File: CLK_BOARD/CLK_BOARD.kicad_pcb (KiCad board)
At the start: 2 copper layers, 18 parts, among them J4 PWR, U1 LMK00804BPW, U2 SN74LVC1G74DCUR, U3 LMK00804BPW, U4 TPS7A9101DSKR, X1 TB612-100.0M

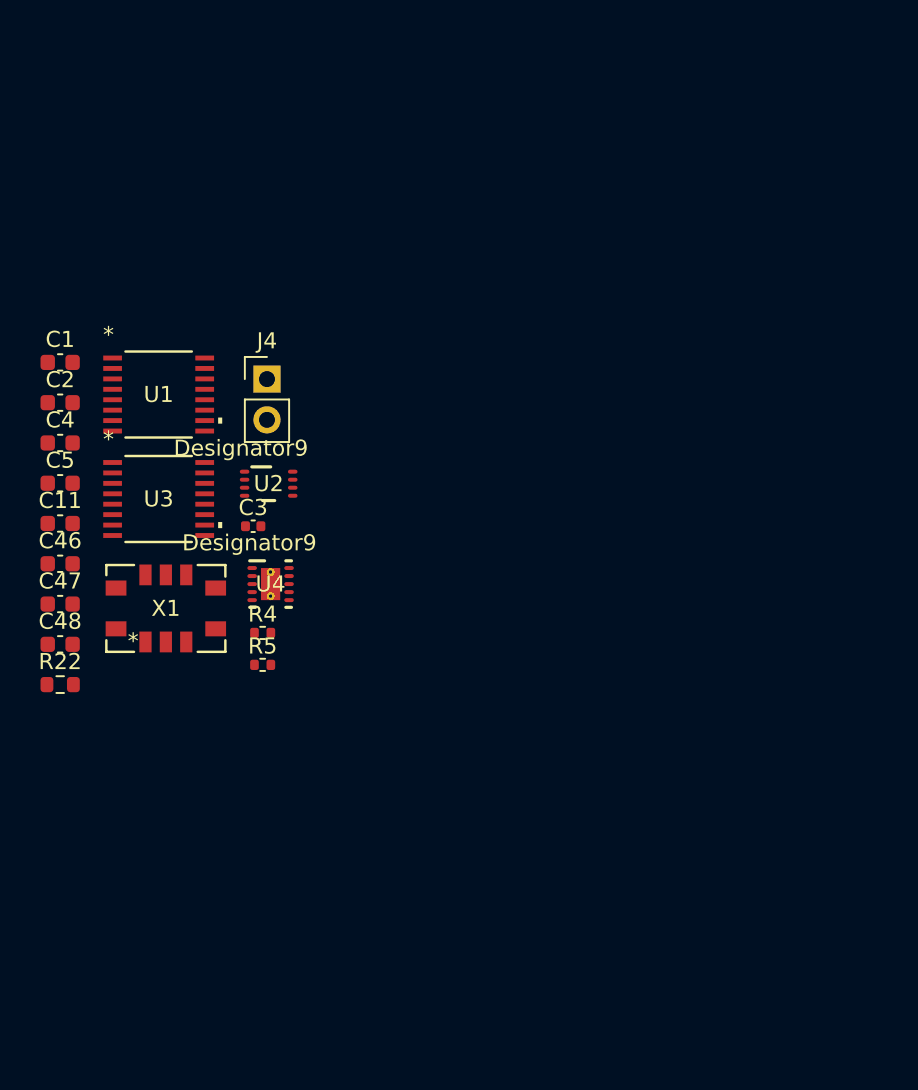
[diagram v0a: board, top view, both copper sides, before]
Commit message: finished clock board schematic
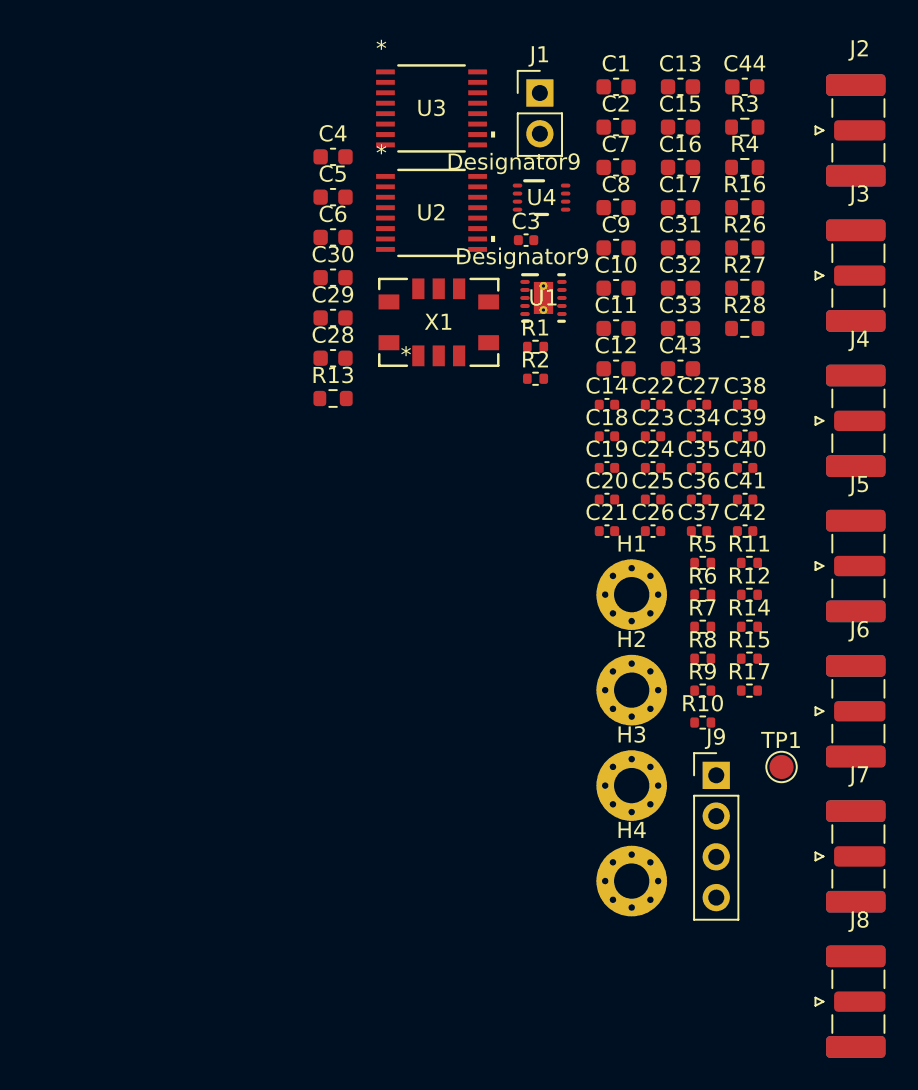
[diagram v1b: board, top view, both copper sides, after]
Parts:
- added C10: 0.1uF, Capacitor_SMD:C_0603_1608Metric, F.Cu at (133.0, 71.5)
- added C11: 0.1uF, Capacitor_SMD:C_0603_1608Metric, F.Cu at (133.0, 74.0)
- added C12: 10uF, Capacitor_SMD:C_0603_1608Metric, F.Cu at (133.0, 76.5)
- added C13: 1uF, Capacitor_SMD:C_0603_1608Metric, F.Cu at (137.0, 58.9)
- added C14: 10nF, Capacitor_SMD:C_0402_1005Metric, F.Cu at (132.4, 78.7)
- added C15: 0.1uF, Capacitor_SMD:C_0603_1608Metric, F.Cu at (137.0, 61.4)
- added C16: 0.1uF, Capacitor_SMD:C_0603_1608Metric, F.Cu at (137.0, 64.0)
- added C17: 0.1uF, Capacitor_SMD:C_0603_1608Metric, F.Cu at (137.0, 66.5)
- added C18: 10nF, Capacitor_SMD:C_0402_1005Metric, F.Cu at (132.4, 80.7)
- added C19: 10nF, Capacitor_SMD:C_0402_1005Metric, F.Cu at (132.4, 82.7)
- added C20: 15pF, Capacitor_SMD:C_0402_1005Metric, F.Cu at (132.4, 84.7)
- added C21: 15pF, Capacitor_SMD:C_0402_1005Metric, F.Cu at (132.4, 86.6)
- added C22: 10nF, Capacitor_SMD:C_0402_1005Metric, F.Cu at (135.3, 78.7)
- added C23: 10nF, Capacitor_SMD:C_0402_1005Metric, F.Cu at (135.3, 80.7)
- added C24: 10nF, Capacitor_SMD:C_0402_1005Metric, F.Cu at (135.3, 82.7)
- added C25: 10nF, Capacitor_SMD:C_0402_1005Metric, F.Cu at (135.3, 84.7)
- added C26: 15pF, Capacitor_SMD:C_0402_1005Metric, F.Cu at (135.3, 86.6)
- added C27: 15pF, Capacitor_SMD:C_0402_1005Metric, F.Cu at (138.2, 78.7)
- added C31: 10uF, Capacitor_SMD:C_0603_1608Metric, F.Cu at (137.0, 69.0)
- added C32: 1uF, Capacitor_SMD:C_0603_1608Metric, F.Cu at (137.0, 71.5)
- added C33: 0.1uF, Capacitor_SMD:C_0603_1608Metric, F.Cu at (137.0, 74.0)
- added C34: 10nF, Capacitor_SMD:C_0402_1005Metric, F.Cu at (138.2, 80.7)
- added C35: 10nF, Capacitor_SMD:C_0402_1005Metric, F.Cu at (138.2, 82.7)
- added C36: 10nF, Capacitor_SMD:C_0402_1005Metric, F.Cu at (138.2, 84.7)
- added C37: 10nF, Capacitor_SMD:C_0402_1005Metric, F.Cu at (138.2, 86.6)
- added C38: 10nF, Capacitor_SMD:C_0402_1005Metric, F.Cu at (141.0, 78.7)
- added C39: 10nF, Capacitor_SMD:C_0402_1005Metric, F.Cu at (141.0, 80.7)
- added C40: 10nF, Capacitor_SMD:C_0402_1005Metric, F.Cu at (141.0, 82.7)
- added C41: 15pF, Capacitor_SMD:C_0402_1005Metric, F.Cu at (141.0, 84.7)
- added C42: 15pF, Capacitor_SMD:C_0402_1005Metric, F.Cu at (141.0, 86.6)
- added C43: 0.1uF, Capacitor_SMD:C_0603_1608Metric, F.Cu at (137.0, 76.5)
- added C44: 0.1uF, Capacitor_SMD:C_0603_1608Metric, F.Cu at (141.0, 58.9)
- added C7: 10uF, Capacitor_SMD:C_0603_1608Metric, F.Cu at (133.0, 64.0)
- added C8: 1uF, Capacitor_SMD:C_0603_1608Metric, F.Cu at (133.0, 66.5)
- added C9: 0.1uF, Capacitor_SMD:C_0603_1608Metric, F.Cu at (133.0, 69.0)
- added H1: MountingHole_Pad, MountingHole:MountingHole_2.2mm_M2_Pad_Via, F.Cu at (134.0, 90.6)
- added H2: MountingHole_Pad, MountingHole:MountingHole_2.2mm_M2_Pad_Via, F.Cu at (134.0, 96.5)
- added H3: MountingHole_Pad, MountingHole:MountingHole_2.2mm_M2_Pad_Via, F.Cu at (134.0, 102.5)
- added H4: MountingHole_Pad, MountingHole:MountingHole_2.2mm_M2_Pad_Via, F.Cu at (134.0, 108.4)
- added J2: OUT_50M_1, Connector_Coaxial:SMA_Samtec_SMA-J-P-H-ST-EM1_EdgeMount, F.Cu at (148.2, 61.6)
- added J3: OUT_50M_2, Connector_Coaxial:SMA_Samtec_SMA-J-P-H-ST-EM1_EdgeMount, F.Cu at (148.2, 70.7)
- added J4: OUT_50M_3, Connector_Coaxial:SMA_Samtec_SMA-J-P-H-ST-EM1_EdgeMount, F.Cu at (148.2, 79.7)
- added J5: OUT_50M_4, Connector_Coaxial:SMA_Samtec_SMA-J-P-H-ST-EM1_EdgeMount, F.Cu at (148.2, 88.8)
- added J6: OUT_100M_3, Connector_Coaxial:SMA_Samtec_SMA-J-P-H-ST-EM1_EdgeMount, F.Cu at (148.2, 97.8)
- added J7: OUT_100M_2, Connector_Coaxial:SMA_Samtec_SMA-J-P-H-ST-EM1_EdgeMount, F.Cu at (148.2, 106.9)
- added J8: OUT_100M_1, Connector_Coaxial:SMA_Samtec_SMA-J-P-H-ST-EM1_EdgeMount, F.Cu at (148.2, 115.9)
- added J9: Conn_01x04, Connector_PinHeader_2.54mm:PinHeader_1x04_P2.54mm_Vertical, F.Cu at (139.2, 101.8)
- added R10: 43, Resistor_SMD:R_0402_1005Metric, F.Cu at (138.4, 98.5)
- added R11: 43, Resistor_SMD:R_0402_1005Metric, F.Cu at (141.3, 88.6)
- added R12: 43, Resistor_SMD:R_0402_1005Metric, F.Cu at (141.3, 90.6)
- added R14: 0, Resistor_SMD:R_0402_1005Metric, F.Cu at (141.3, 92.6)
- added R15: 0, Resistor_SMD:R_0402_1005Metric, F.Cu at (141.3, 94.6)
- added R16: 0, Resistor_SMD:R_0603_1608Metric, F.Cu at (141.0, 66.5)
- added R17: 0, Resistor_SMD:R_0402_1005Metric, F.Cu at (141.3, 96.6)
- added R26: 10k, Resistor_SMD:R_0603_1608Metric, F.Cu at (141.0, 69.0)
- added R27: 10k, Resistor_SMD:R_0603_1608Metric, F.Cu at (141.0, 71.5)
- added R28: 100k, Resistor_SMD:R_0603_1608Metric, F.Cu at (141.0, 74.0)
- added R3: 0, Resistor_SMD:R_0603_1608Metric, F.Cu at (141.0, 61.4)
- added R4: 0, Resistor_SMD:R_0603_1608Metric, F.Cu at (141.0, 64.0)
- added R5: 43, Resistor_SMD:R_0402_1005Metric, F.Cu at (138.4, 88.6)
- added R6: 43, Resistor_SMD:R_0402_1005Metric, F.Cu at (138.4, 90.6)
- added R7: 43, Resistor_SMD:R_0402_1005Metric, F.Cu at (138.4, 92.6)
- added R8: 0, Resistor_SMD:R_0402_1005Metric, F.Cu at (138.4, 94.6)
- added R9: 43, Resistor_SMD:R_0402_1005Metric, F.Cu at (138.4, 96.6)
- added TP1: PG, TestPoint:TestPoint_Pad_D1.5mm, F.Cu at (143.3, 101.3)
- C1: value 0.1uF -> 10uF
- C2: value 10uF -> 0.1uF
- moved C1 38.7 mm to (133.0, 58.9)
- moved C2 38.7 mm to (133.0, 61.4)
- moved U4 24.6 mm to (128.4, 65.8)
- moved U3 24.6 mm to (121.5, 60.3)
- moved C29 24.6 mm to (115.4, 73.3)
- moved C5 24.6 mm to (115.4, 65.8)
- moved R1 24.6 mm to (128.0, 75.1)
- moved R2 24.6 mm to (128.0, 77.1)
- moved U1 24.6 mm to (128.5, 72.1)
- moved U2 24.6 mm to (121.5, 66.8)
- moved X1 24.6 mm to (122.0, 73.6)
- moved C28 24.6 mm to (115.4, 75.8)
- moved C3 24.6 mm to (127.4, 68.5)
- moved C30 24.6 mm to (115.4, 70.8)
- moved C4 24.6 mm to (115.4, 63.3)
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- renumbered C48 to C28, C47 to C29, C46 to C30, C11 to C6, J4 to J1, R4 to R1, R22 to R13, R5 to R2, U4 to U1, U3 to U2, U1 to U3, U2 to U4
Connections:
- U1 pad 5: GND -> Net-(U1-PG)
- U2 pad 4: unconnected-(U3-CLK_EN-Pad4) -> /nMUTE
- U2 pad 7: unconnected-(U3-CLK_SEL-Pad7) -> GND
- U2 pad 8: Net-(U2-D) -> Net-(U2-LVCMOS_CLK)
- U3 pad 16: Net-(U1-Q0) -> Net-(U3-Q0)
- U3 pad 4: unconnected-(U1-CLK_EN-Pad4) -> /nMUTE
- U3 pad 8: Net-(U1-LVCMOS_CLK) -> /OSC_OUT
- U4 pad 1: Net-(U1-Q0) -> Net-(U4-CLK)
- U4 pad 2: Net-(U2-D) -> Net-(U4-D)
- U4 pad 3: Net-(U2-D) -> Net-(U4-D)
- U4 pad 5: unconnected-(U2-Q-Pad5) -> Net-(U4-Q)
- U4 pad 6: unconnected-(U2-CLR_N-Pad6) -> /nRST
- U4 pad 7: unconnected-(U2-PRE_N-Pad7) -> Net-(U4-PRE_N)
- U4 pad 8: unconnected-(U2-VCC-Pad8) -> Net-(U4-VCC)
- X1 pad 5: Net-(U1-LVCMOS_CLK) -> Net-(X1-OUTPUT)

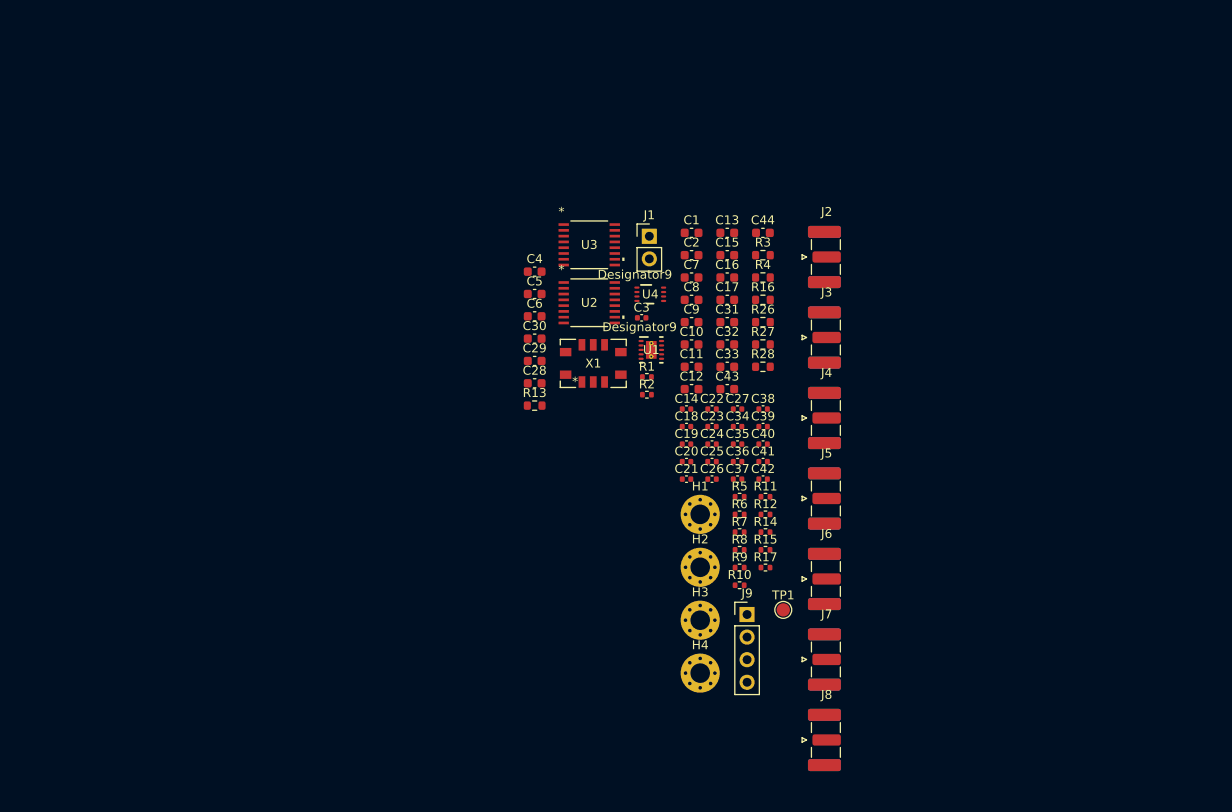
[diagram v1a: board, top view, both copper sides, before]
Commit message: started layout of clk distribution board
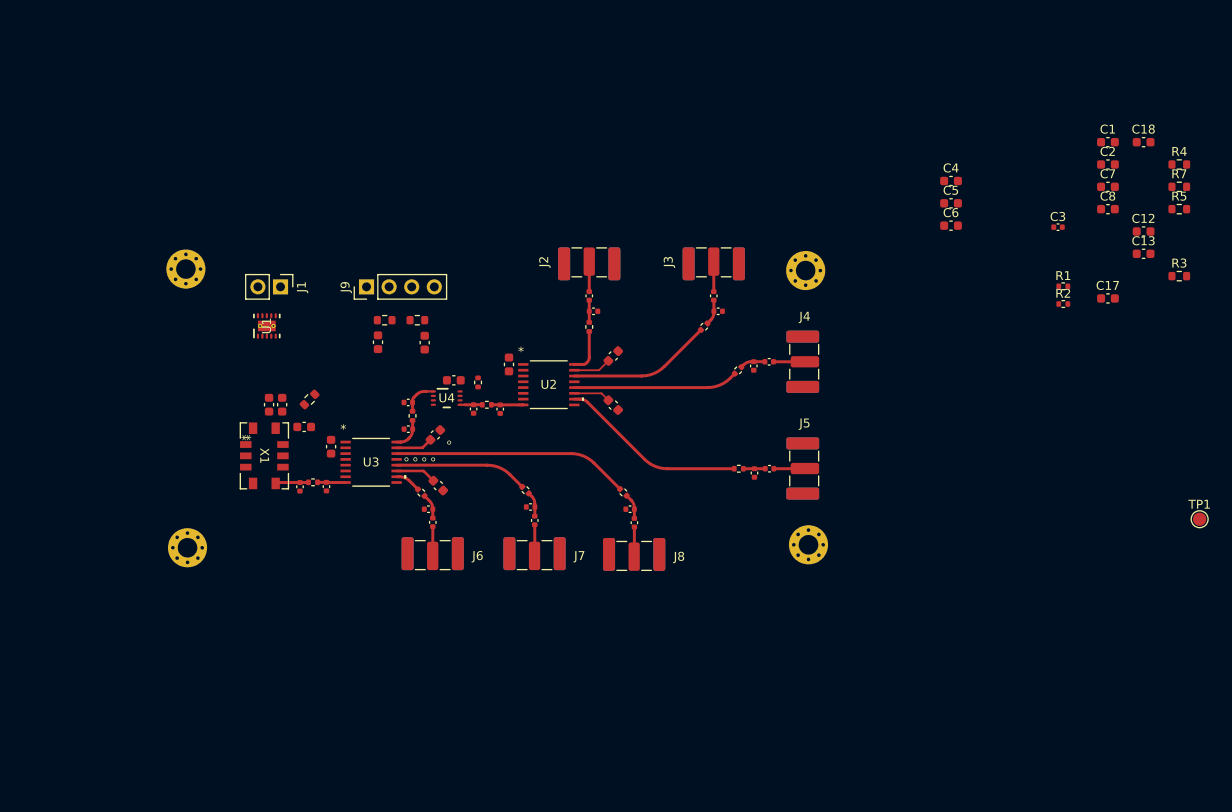
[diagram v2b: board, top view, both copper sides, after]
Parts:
- removed the C29 at (115.4, 73.3)
- removed the C30 at (115.4, 70.8)
- added C43: 0.1uF, Capacitor_SMD:C_0603_1608Metric, F.Cu at (87.0, 78.2)
- added C44: 10nF, Capacitor_SMD:C_0603_1608Metric, F.Cu at (85.5, 78.2)
- moved H1 64.1 mm to (76.2, 63.0)
- moved H3 58.2 mm to (76.3, 94.3)
- moved J9 56.5 mm to (96.5, 65.0), turned to 90 degrees
- moved R20 51.2 mm to (90.4, 87.0)
- moved C1 47.9 mm to (179.8, 48.7)
- moved C12 47.9 mm to (183.8, 58.8)
- moved C13 47.9 mm to (183.8, 61.3)
- moved C17 47.9 mm to (179.8, 66.3)
- moved C18 47.9 mm to (183.8, 48.7)
- moved C2 47.9 mm to (179.8, 51.2)
- moved C3 47.9 mm to (174.2, 58.3)
- moved C4 47.9 mm to (162.2, 53.1)
- moved C5 47.9 mm to (162.2, 55.6)
- moved C6 47.9 mm to (162.2, 58.1)
- moved C7 47.9 mm to (179.8, 53.8)
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- renumbered C31 to C12, C32 to C13, C33 to C14, C14 to C15, C34 to C16, C12 to C17, C13 to C18, C15 to C19, C16 to C20, C17 to C21, C18 to C22, C35 to C23, C20 to C24, C21 to C25, C41 to C26, C42 to C27, C19 to C28, C36 to C29, C22 to C30, C37 to C31, C40 to C32, C39 to C33, C38 to C34, C23 to C35, C24 to C36, C25 to C37, C44 to C38, C43 to C39, C26 to C40, C27 to C41, C28 to C42, R17 to R10, R7 to R11, R15 to R12, R9 to R13, R10 to R14, R11 to R15, R12 to R16, R26 to R17, R27 to R18, R13 to R19, R14 to R20, R28 to R3, R3 to R4, R16 to R5, R5 to R6, R4 to R7, R6 to R8, R8 to R9
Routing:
- net Net-(U3-Q1): track 0.00 -> 26.6 mm
- net Net-(U2-Q3): track 0.00 -> 21.0 mm
- net Net-(U2-Q2): track 0.00 -> 18.5 mm
- net Net-(U2-Q1): track 0.00 -> 16.2 mm
- net Net-(U3-Q2): track 0.00 -> 15.0 mm
- net Net-(U3-VDD): track 0.00 -> 8.77 mm
- net Net-(U2-VDD): track 0.00 -> 8.42 mm
- net Net-(U2-Q0): track 0.00 -> 5.05 mm
- net Net-(U4-CLK): track 0.00 -> 4.02 mm
- net Net-(X1-OUTPUT): track 0.00 -> 3.74 mm
- net Net-(U3-Q0): track 0.00 -> 3.62 mm
- net Net-(U2-LVCMOS_CLK): track 0.00 -> 3.59 mm
- net Net-(J4-In): track 0.00 -> 3.54 mm
- net Net-(J7-In): track 0.00 -> 3.51 mm
- net Net-(J5-In): track 0.00 -> 3.51 mm
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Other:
- copper layers 2 -> 4

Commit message: moved from TSSOP to QFN to make the pcb smaller, will have to restart layout
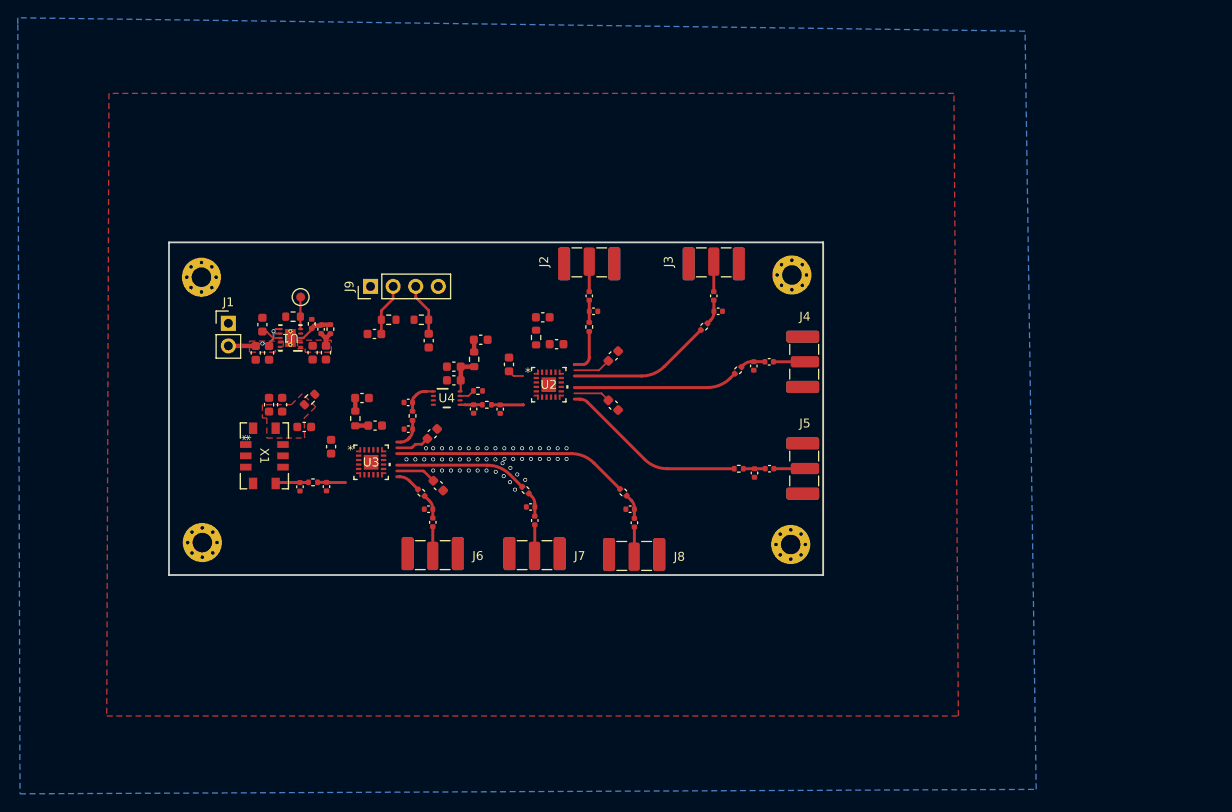
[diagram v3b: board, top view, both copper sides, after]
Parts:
- U2, U3: value LMK00804BPW -> LMK00804BQWRGTRQ1; footprint Snapeda:PW16_TEX-L -> Snapeda:VQFN16_RGT_TEX
- moved TP1 104.1 mm to (89.0, 66.2)
- moved R3 99.7 mm to (88.2, 68.3)
- moved C2 98.1 mm to (84.0, 72.4), turned to -90 degrees
- moved C1 97.2 mm to (85.5, 72.4), turned to -90 degrees
- moved R7 96.2 mm to (95.2, 79.8), turned to -90 degrees
- moved C18 92.1 mm to (97.4, 80.6)
- moved C17 84.6 mm to (96.0, 77.5)
- moved R2 84.5 mm to (90.3, 69.2), turned to 90 degrees
- moved C3 83.6 mm to (91.3, 69.8), turned to 90 degrees
- moved R1 82.5 mm to (92.4, 69.8), turned to 90 degrees
- moved R5 81.1 mm to (108.6, 73.2), turned to -90 degrees
- moved C13 78.6 mm to (106.3, 74.0), turned to 180 degrees
- moved C6 78.2 mm to (84.8, 69.2), turned to 90 degrees
- moved C12 75.5 mm to (109.3, 71.0)
- moved R4 74.9 mm to (115.5, 70.7), turned to -90 degrees
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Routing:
- net Net-(J1-Pin_2): track 0.00 -> 7.07 mm, vias 0 -> 2
- net +3V3: track 0.00 -> 6.04 mm
- net /nRST: track 0.00 -> 5.93 mm
- net /nMUTE: track 0.00 -> 5.90 mm
- net Net-(U4-VCC): track 0.00 -> 4.36 mm
- net Net-(U1-FB): track 0.00 -> 3.94 mm
- net Net-(U1-PG): track 0.00 -> 3.62 mm
- net Net-(U1-NR_SS): track 0.00 -> 2.30 mm
- net Net-(U2-VDD): track 8.42 -> 10.2 mm
- net Net-(U4-PRE_N): track 0.00 -> 1.74 mm
- net Net-(U3-VDD): track 8.77 -> 9.93 mm
- net GND: vias 0 -> 51
- net (no net): vias 5 -> 0
- added copper zone on F.Cu, net +3V3
- added copper zone on B.Cu, net GND
- added copper zone on F.Cu, net GND
- added copper zone on In1.Cu, net GND
- added copper zone on In2.Cu, net GND
- added copper zone on F.Cu, net Net-(J1-Pin_2)
- added copper zone on F.Cu, net Net-(X1-VCC)
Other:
- board outline added: 73.6 x 37.4 mm
